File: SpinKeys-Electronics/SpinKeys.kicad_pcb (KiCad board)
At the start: 2 copper layers, 73.5 x 72.5 mm, 14 parts, among them SW1 SW_Push, SW2 SW_Push, SW3 SW_Push, SW4 SW_Push, SW5 SW_Push, U1 XIAO-RP2040-DIP

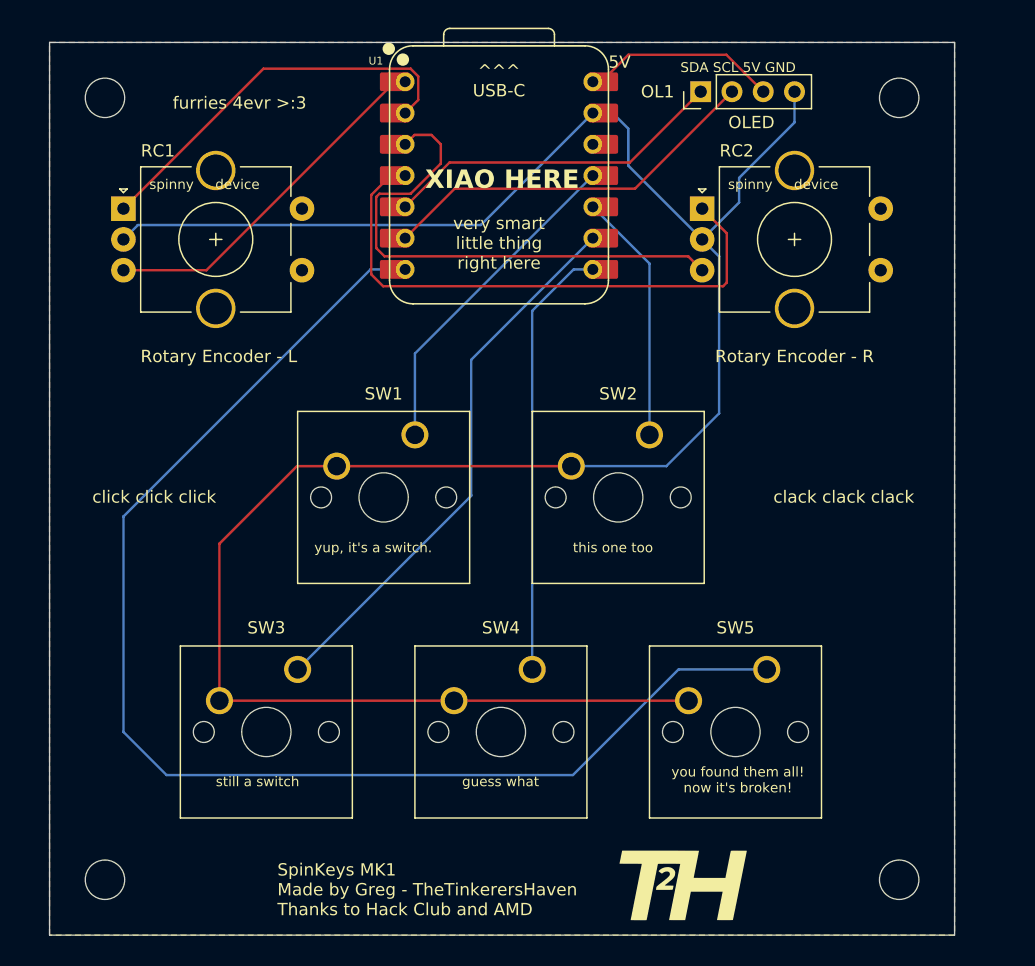
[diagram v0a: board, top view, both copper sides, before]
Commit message: Update PCB layout and silkscreen for SpinKeys MK1
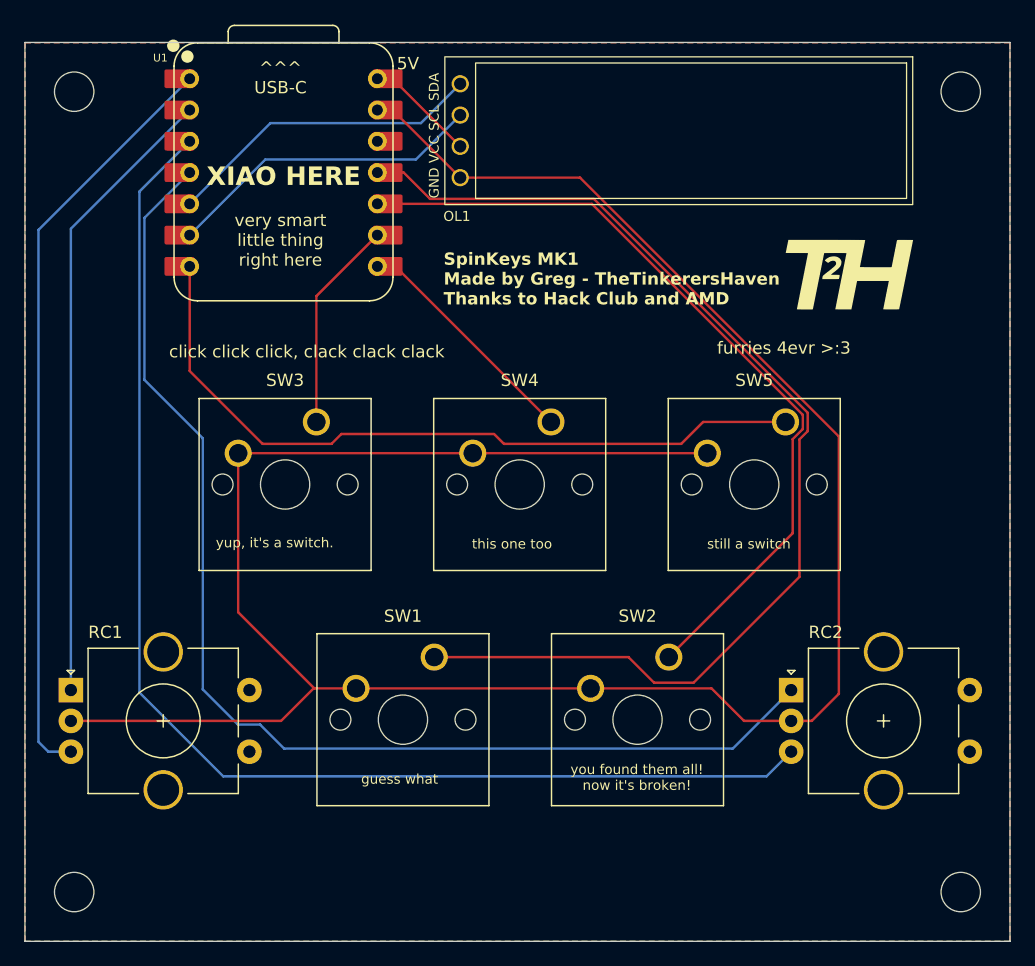
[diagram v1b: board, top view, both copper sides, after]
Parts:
- OL1: footprint Connector_PinHeader_2.54mm:PinHeader_1x04_P2.54mm_Vertical -> KBD:OLED
- moved G*** 51.4 mm to (135.5, 41.9)
- moved RC2 39.8 mm to (130.7, 75.6)
- moved RC1 39.3 mm to (72.2, 75.6)
- moved SW3 20.2 mm to (92.2, 53.8)
- moved SW5 20.2 mm to (130.3, 53.8)
- moved SW4 20.2 mm to (111.2, 53.8)
- moved OL1 19.8 mm to (103.8, 30.2), turned to -90 degrees
- moved SW2 18.1 mm to (120.8, 72.9)
- moved SW1 18.1 mm to (101.7, 72.9)
- moved U1 17.5 mm to (89.5, 33.6)
- moved REF** 5.10 mm to (144.5, 92.0)
- moved REF** 5.02 mm to (144.5, 27.0)
- moved REF** 2.69 mm to (72.5, 92.0)
- moved REF** 2.55 mm to (72.5, 27.0)
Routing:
- net Net-(U1-GPIO3/MOSI): track 27.0 -> 89.9 mm
- net Net-(U1-GPIO28/ADC2/A2): track 42.8 -> 103.0 mm
- net Net-(U1-GPIO29/ADC3/A3): track 44.9 -> 97.2 mm
- net Net-(U1-GPIO0/TX): track 105.9 -> 60.7 mm
- net Net-(U1-GPIO4/MISO): track 20.4 -> 65.0 mm
- net Net-(U1-GPIO26/ADC0/A0): track 28.4 -> 61.9 mm
- net Net-(U1-GPIO2/SCK): track 45.0 -> 17.2 mm
- net Net-(U1-GPIO27/ADC1/A1): track 32.3 -> 51.1 mm
- net Net-(U1-GPIO1/RX): track 35.4 -> 17.9 mm
- net GND: track 182.9 -> 193.4 mm
- net +5V: track 15.1 -> 7.77 mm
- net Net-(OL1-SCL): track 31.5 -> 26.0 mm
- net Net-(OL1-SDA): track 27.9 -> 26.0 mm
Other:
- board size 73.5 x 72.5 mm -> 80 x 73 mm
- board text added: "GND VCC SCL SDA"
- board text added: "click click click, clack clack clack"
- board text removed: "Rotary Encoder - L"
- board text removed: "Rotary Encoder - R"
- board text removed: "SDA SCL 5V GND"
- board text removed: "clack clack clack"
- board text removed: "click click click"
- board text removed: "spinny device"

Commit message: Upload STEP files, update PCB to final
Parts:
- moved RC2 0.68 mm to (130.1, 75.6)
- moved RC1 0.28 mm to (72.0, 75.6)
- moved SW5 0.14 mm to (130.1, 53.8)
- moved SW1 0.14 mm to (101.6, 72.9)
- moved SW2 0.14 mm to (120.7, 72.9)
- moved SW3 0.14 mm to (92.0, 53.8)
- moved SW4 0.14 mm to (111.1, 53.8)
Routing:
- net Net-(U1-GPIO28/ADC2/A2): track 103.0 -> 103.8 mm
- net Net-(U1-GPIO29/ADC3/A3): track 97.2 -> 96.5 mm
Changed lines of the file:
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@@
 	(footprint "Button_Switch_Keyboard:SW_Cherry_MX_1.00u_PCB"
 		(layer "F.Cu")
-		(at 130.27 53.82)
+		(at 130.13 53.82)
 		(descr "Cherry MX keyswitch, 1.00u, PCB mount, http://cherryamericas.com/wp-content/uploads/2014/12/mx_cat.pdf")
 		(tags "Cherry MX keyswitch 1.00u PCB")
@@
 	(footprint "Rotary_Encoder:RotaryEncoder_Alps_EC11E-Switch_Vertical_H20mm_CircularMountingHoles"
 		(layer "F.Cu")
-		(at 72.23 75.6)
+		(at 71.95 75.6)
 		(descr "Alps rotary encoder, EC11E... with switch, vertical shaft, mounting holes with circular drills, http://www.alps.com/prod/info/E/HTML/Encoder/Incremental/EC11/EC11E15204A3.html")
 		(tags "rotary encoder")
@@
 	(footprint "Button_Switch_Keyboard:SW_Cherry_MX_1.00u_PCB"
 		(layer "F.Cu")
-		(at 101.74 72.92)
+		(at 101.6 72.92)
 		(descr "Cherry MX keyswitch, 1.00u, PCB mount, http://cherryamericas.com/wp-content/uploads/2014/12/mx_cat.pdf")
 		(tags "Cherry MX keyswitch 1.00u PCB")
@@
 	(footprint "Button_Switch_Keyboard:SW_Cherry_MX_1.00u_PCB"
 		(layer "F.Cu")
-		(at 120.79 72.92)
+		(at 120.65 72.92)
 		(descr "Cherry MX keyswitch, 1.00u, PCB mount, http://cherryamericas.com/wp-content/uploads/2014/12/mx_cat.pdf")
 		(tags "Cherry MX keyswitch 1.00u PCB")
@@
 	(footprint "Rotary_Encoder:RotaryEncoder_Alps_EC11E-Switch_Vertical_H20mm_CircularMountingHoles"
 		(layer "F.Cu")
-		(at 130.73 75.6)
+		(at 130.05 75.6)
 		(descr "Alps rotary encoder, EC11E... with switch, vertical shaft, mounting holes with circular drills, http://www.alps.com/prod/info/E/HTML/Encoder/Incremental/EC11/EC11E15204A3.html")
 		(tags "rotary encoder")
@@
 	(footprint "Button_Switch_Keyboard:SW_Cherry_MX_1.00u_PCB"
 		(layer "F.Cu")
-		(at 92.17 53.82)
+		(at 92.03 53.82)
 		(descr "Cherry MX keyswitch, 1.00u, PCB mount, http://cherryamericas.com/wp-content/uploads/2014/12/mx_cat.pdf")
 		(tags "Cherry MX keyswitch 1.00u PCB")
@@
 	(footprint "Button_Switch_Keyboard:SW_Cherry_MX_1.00u_PCB"
 		(layer "F.Cu")
-		(at 111.22 53.82)
+		(at 111.08 53.82)
 		(descr "Cherry MX keyswitch, 1.00u, PCB mount, http://cherryamericas.com/wp-content/uploads/2014/12/mx_cat.pdf")
 		(tags "Cherry MX keyswitch 1.00u PCB")
@@
 	)
 	(segment
-		(start 125.979 80.351)
+		(start 125.299 80.351)
 		(end 89.551 80.351)
 		(width 0.2)
@@
 	)
 	(segment
+		(start 130.05 75.6)
+		(end 125.299 80.351)
+		(width 0.2)
+		(layer "B.Cu")
+		(net 13)
+	)
+	(segment
 		(start 87.6 78.4)
 		(end 85.8 78.4)
@@
 	)
 	(segment
-		(start 130.73 75.6)
-		(end 125.979 80.351)
-		(width 0.2)
-		(layer "B.Cu")
-		(net 13)
-	)
-	(segment
 		(start 82.943 75.543)
 		(end 82.943 55.143)
@@
 	)
 	(segment
-		(start 130.73 80.6)
-		(end 128.73 82.6)
+		(start 84.6 82.6)
+		(end 76 74)
 		(width 0.2)
 		(layer "B.Cu")
@@
 	)
 	(segment
-		(start 77.799 75.799)
-		(end 77.799 35.1095)
+		(start 76 36.9085)
+		(end 81.88 31.0285)
 		(width 0.2)
 		(layer "B.Cu")
@@
 	)
 	(segment
-		(start 77.799 35.1095)
-		(end 81.88 31.0285)
+		(start 76 74)
+		(end 76 36.9085)
 		(width 0.2)
 		(layer "B.Cu")
@@
 	)
 	(segment
-		(start 84.6 82.6)
-		(end 77.799 75.799)
+		(start 128.05 82.6)
+		(end 84.6 82.6)
 		(width 0.2)
 		(layer "B.Cu")
@@
 	)
 	(segment
-		(start 128.73 82.6)
-		(end 84.6 82.6)
+		(start 130.05 80.6)
+		(end 128.05 82.6)
 		(width 0.2)
 		(layer "B.Cu")
